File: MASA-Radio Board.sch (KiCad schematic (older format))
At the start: 47 parts, among them IC1 FAN4010IL6X_F113, IC2 FAN4010IL6X_F113, J1 SC_19-20, J2 Conn_01x03_Male, J3 Conn_01x02, J4 Conn_01x06, J5 Conn_01x06, J6 Conn_01x02, J7 UJ2-MBH-1-SMT-TR, J8 Conn_01x02_Male, U1 MP5077GG-Z, U2 MIC5504-3.3YM5-TR, U3 BL654PA, U4 XBP9B-DPST-001, U6 MP5077GG-Z

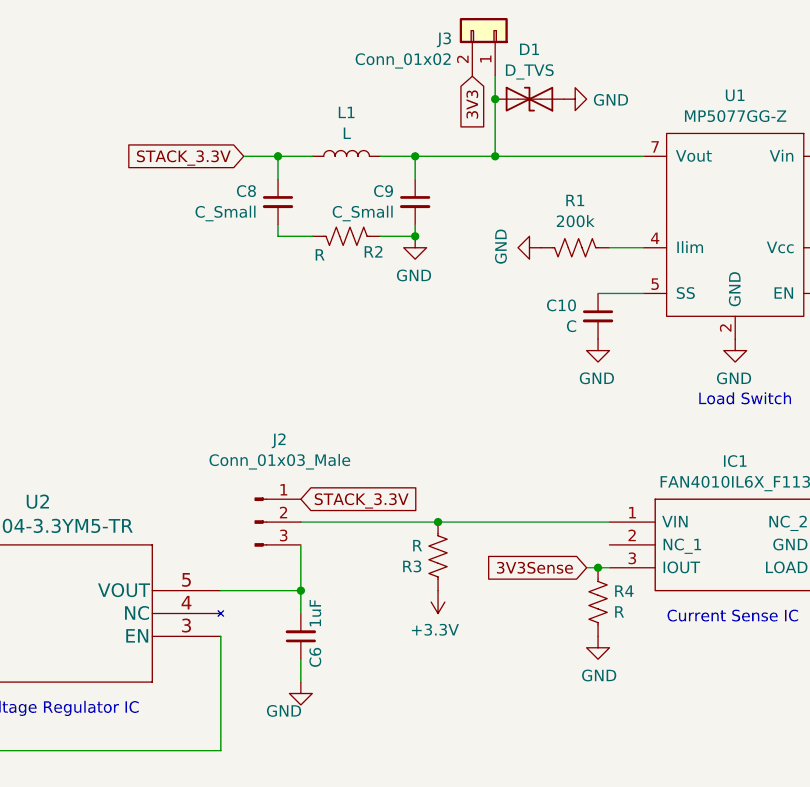
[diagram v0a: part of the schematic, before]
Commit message: Updated R/Cap values
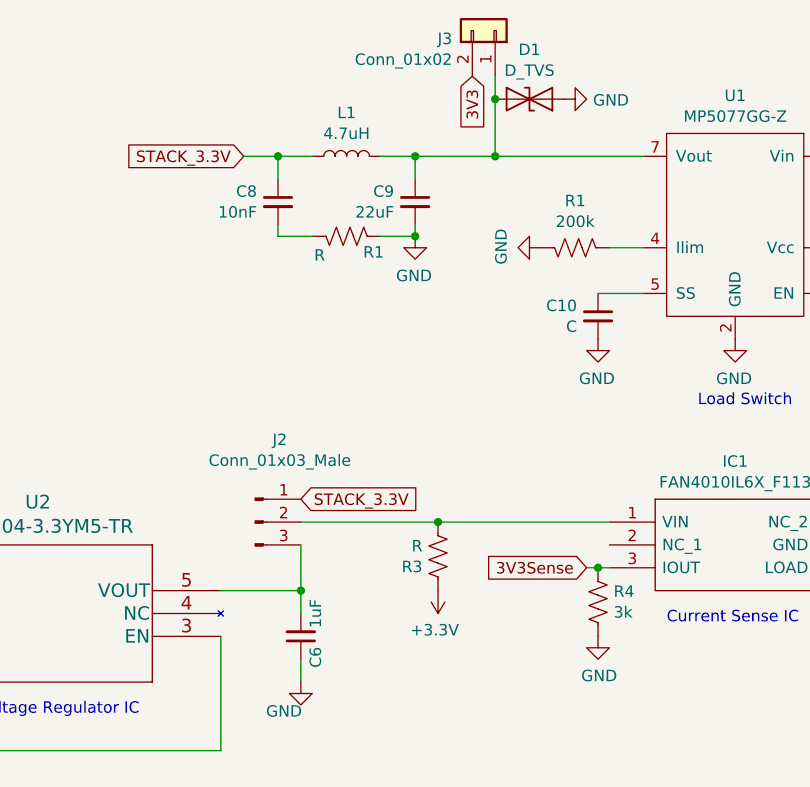
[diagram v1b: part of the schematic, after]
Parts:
- C8: value C_Small -> 10nF
- C9: value C_Small -> 22uF
- L1: value L -> 4.7uH
- R4: value R -> 3k
- renumbered R2 to R1
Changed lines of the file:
@@
 P 6450 4500
 F 0 "R4" H 6518 4546 50  0000 L CNN
-F 1 "R" H 6518 4455 50  0000 L CNN
+F 1 "3k" H 6518 4455 50  0000 L CNN
 F 2 "" V 6490 4490 50  0001 C CNN
 F 3 "~" H 6450 4500 50  0001 C CNN
@@
 	5650 2850 5650 2900
 $Comp
-L Device:R_US R2
+L Device:R_US R1
 U 1 1 5E0D0355
 P 5350 2900
-F 0 "R2" V 5280 3018 50  0000 C CNN
+F 0 "R1" V 5280 3018 50  0000 C CNN
 F 1 "R" V 5267 2782 50  0000 C CNN
 F 2 "" V 5390 2890 50  0001 C CNN
@@
 P 5350 2550
 F 0 "L1" V 5540 2550 50  0000 C CNN
-F 1 "L" V 5449 2550 50  0000 C CNN
+F 1 "4.7uH" V 5449 2550 50  0000 C CNN
 F 2 "" H 5350 2550 50  0001 C CNN
 F 3 "~" H 5350 2550 50  0001 C CNN
@@
 P 5650 2750
 F 0 "C9" H 5742 2796 50  0000 L CNN
-F 1 "C_Small" H 5742 2705 50  0000 L CNN
+F 1 "22uF" H 5742 2705 50  0000 L CNN
 F 2 "" H 5650 2750 50  0001 C CNN
 F 3 "~" H 5650 2750 50  0001 C CNN
@@
 P 5050 2750
 F 0 "C8" H 5142 2796 50  0000 L CNN
-F 1 "C_Small" H 5142 2705 50  0000 L CNN
+F 1 "10nF" H 5142 2705 50  0000 L CNN
 F 2 "" H 5050 2750 50  0001 C CNN
 F 3 "~" H 5050 2750 50  0001 C CNN

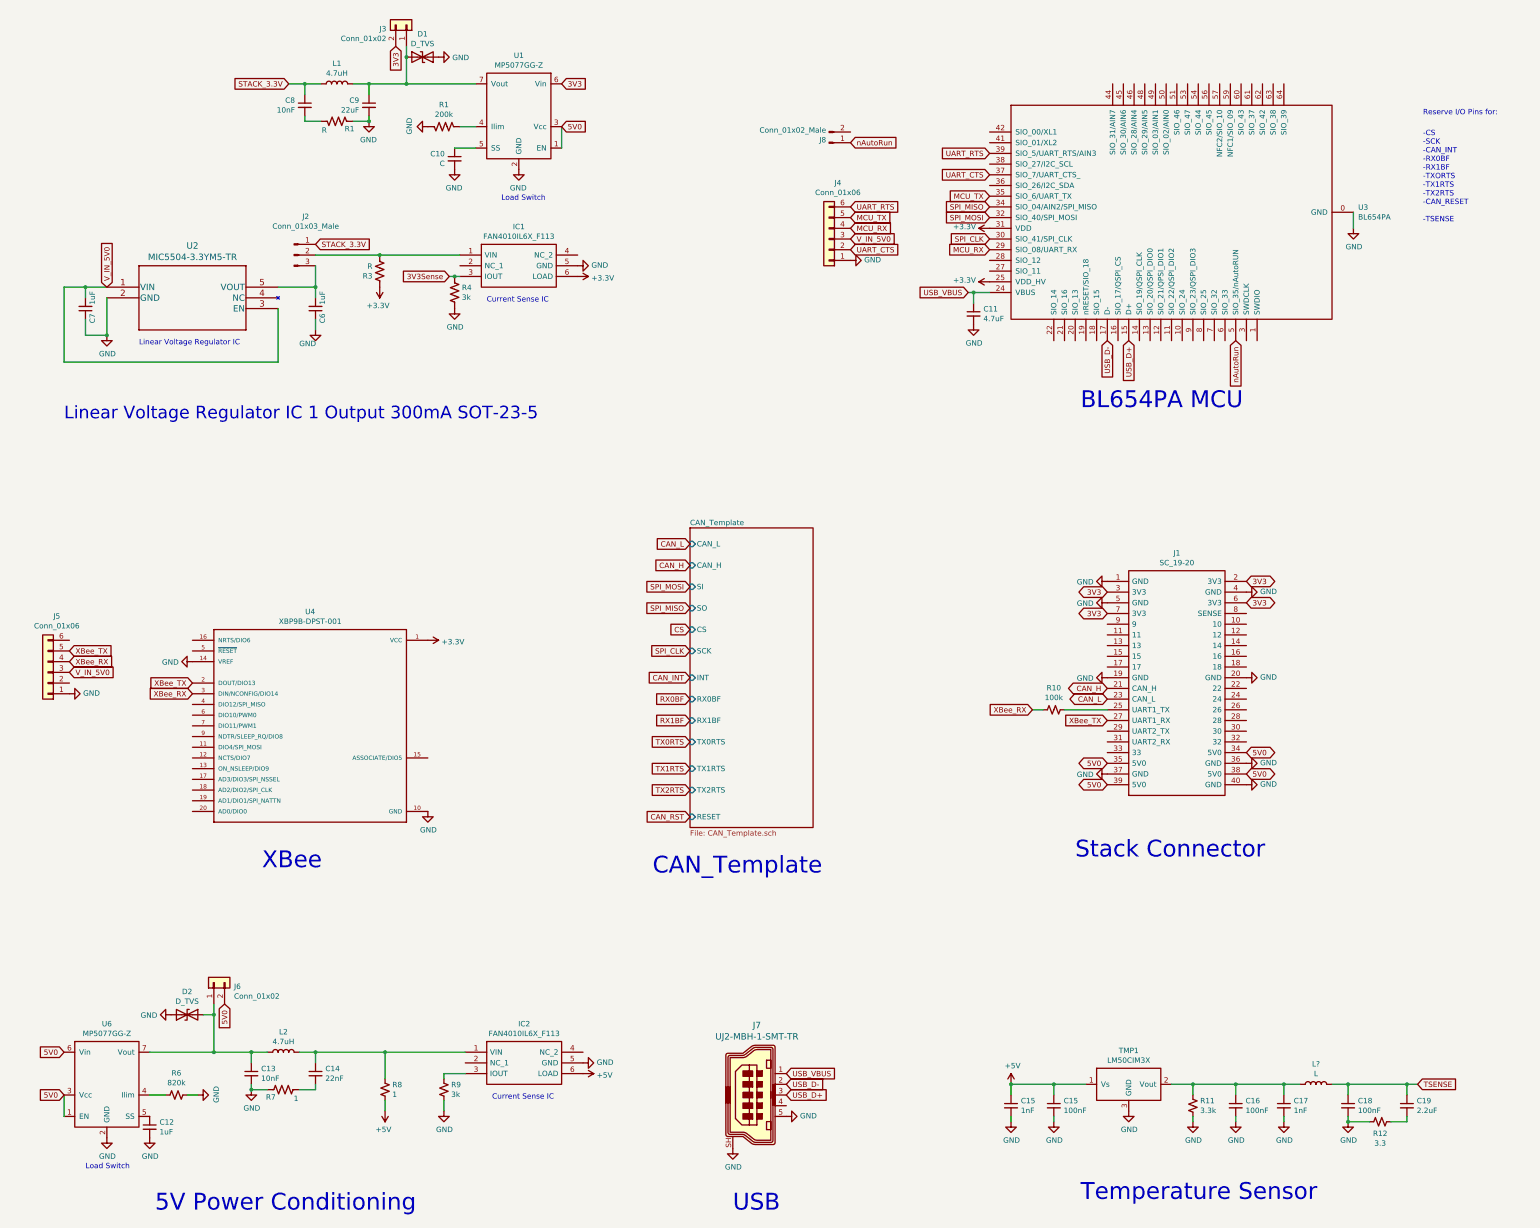
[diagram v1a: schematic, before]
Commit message: Some minor footprint and value updates - unfinished
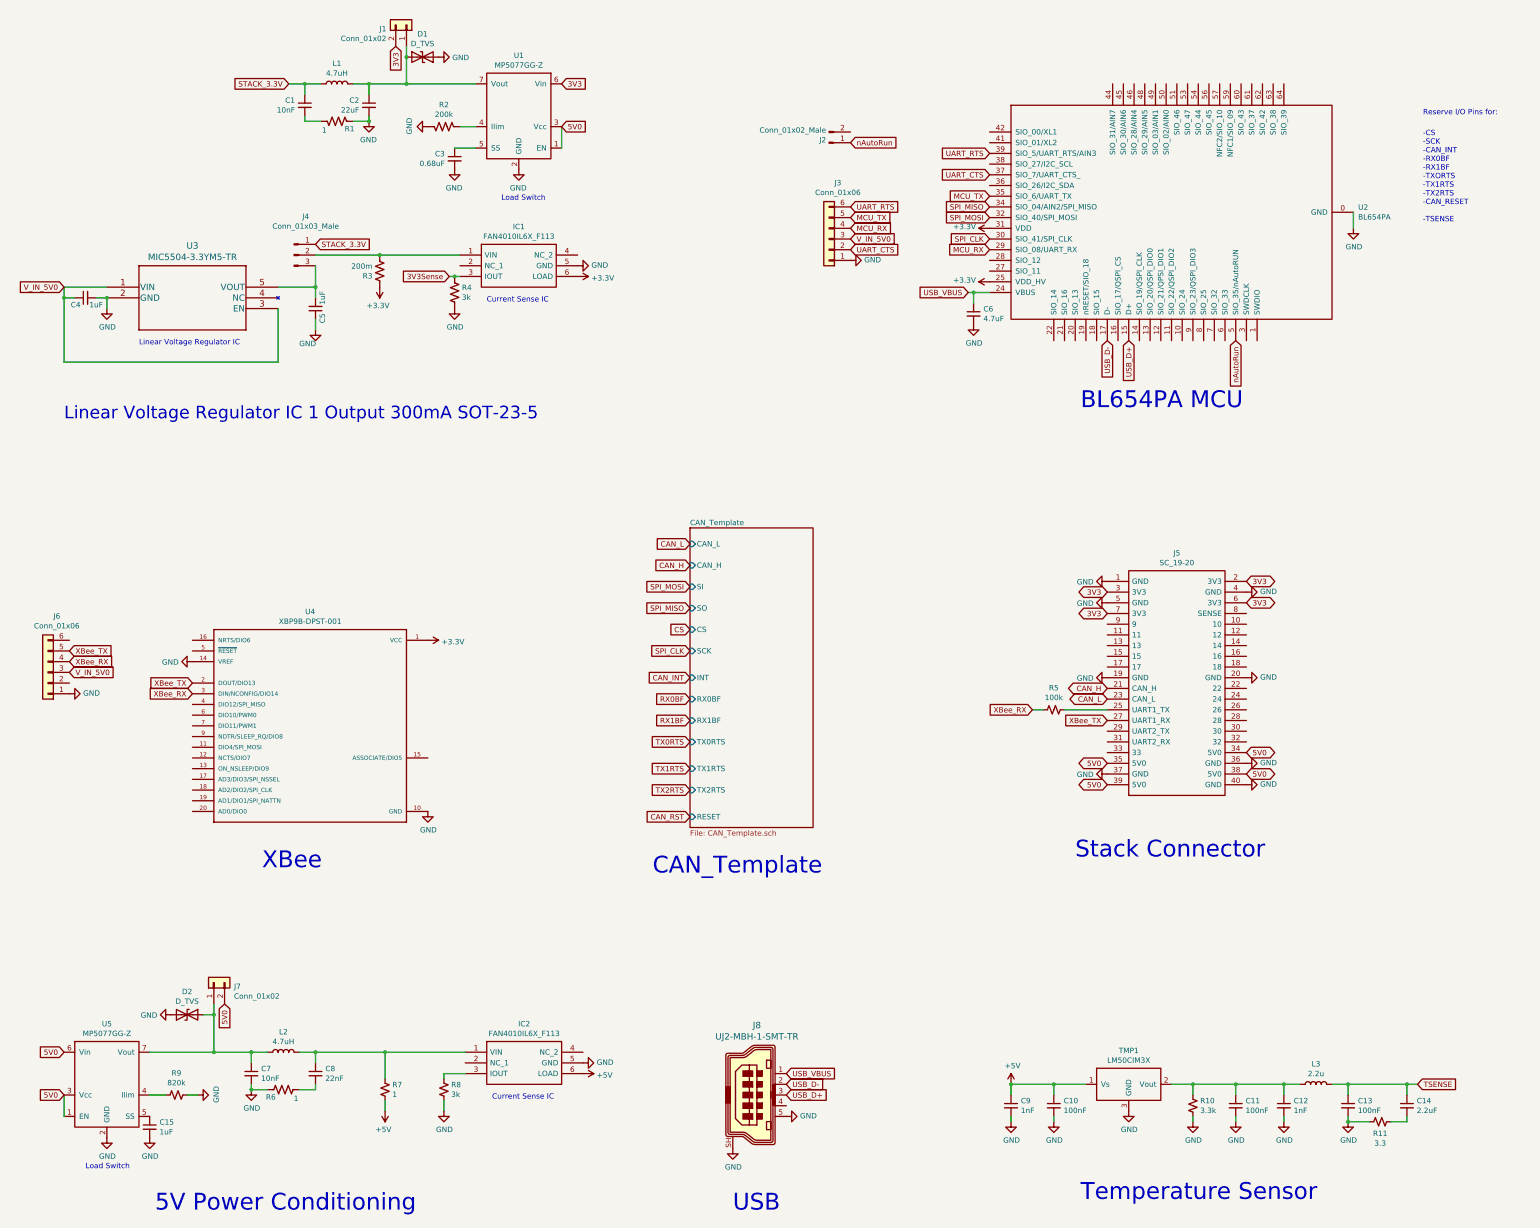
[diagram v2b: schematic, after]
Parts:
- C1: renamed from C8; footprint (none) -> Capacitor_SMD:C_0402_1005Metric
- C10, C9: renamed from C15; footprint (none) -> Capacitor_SMD:C_0805_2012Metric
- C11: renamed from C16; footprint (none) -> Capacitor_SMD:C_0805_2012Metric
- C12: renamed from C17; footprint (none) -> Capacitor_SMD:C_0805_2012Metric
- C13: renamed from C18; footprint (none) -> Capacitor_SMD:C_0805_2012Metric
- C14: renamed from C19; footprint (none) -> Capacitor_SMD:C_0805_2012Metric
- C15: renamed from C12; footprint (none) -> Capacitor_SMD:C_0805_2012Metric
- C2: renamed from C9; footprint (none) -> Capacitor_SMD:C_0805_2012Metric
- C3: renamed from C10; value C -> 0.68uF; footprint (none) -> Capacitor_SMD:C_0805_2012Metric
- C4: renamed from C7; footprint (none) -> Capacitor_SMD:C_0805_2012Metric
- C5: renamed from C6; footprint (none) -> Capacitor_SMD:C_0805_2012Metric
- C6: renamed from C11; footprint (none) -> Capacitor_SMD:C_0805_2012Metric
- C7: renamed from C13; footprint (none) -> Capacitor_SMD:C_0402_1005Metric
- C8: renamed from C14; footprint (none) -> Capacitor_SMD:C_0805_2012Metric
- L1, L2: footprint (none) -> Inductor_SMD:L_0805_2012Metric
- L3: renamed from L?; value L -> 2.2u; footprint (none) -> Inductor_SMD:L_0805_2012Metric
- R1: value R -> 1; footprint (none) -> Resistor_SMD:R_0402_1005Metric
- R10: renamed from R11; footprint (none) -> Resistor_SMD:R_0805_2012Metric
- R11: renamed from R12; footprint (none) -> Resistor_SMD:R_0805_2012Metric
- R2: renamed from R1; footprint (none) -> Resistor_SMD:R_0805_2012Metric
- R3: value R -> 200m; footprint (none) -> Resistor_SMD:R_0805_2012Metric
- R4: footprint (none) -> Resistor_SMD:R_0805_2012Metric
- R5: renamed from R10; footprint (none) -> Resistor_SMD:R_0805_2012Metric
- R6: renamed from R7; footprint (none) -> Resistor_SMD:R_0402_1005Metric
- R7: renamed from R8; footprint (none) -> Resistor_SMD:R_0805_2012Metric
- R8: renamed from R9; footprint (none) -> Resistor_SMD:R_0805_2012Metric
- R9: renamed from R6; footprint (none) -> Resistor_SMD:R_0805_2012Metric
- renumbered J3 to J1, J8 to J2, J4 to J3, J2 to J4, J1 to J5, J5 to J6, J6 to J7, J7 to J8, U3 to U2, U2 to U3, U6 to U5
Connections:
- net GND: now also C4.2; no longer C4.1
- net V_IN_5V0: now also C4.1; no longer C4.2
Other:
- moved on the sheet: C4

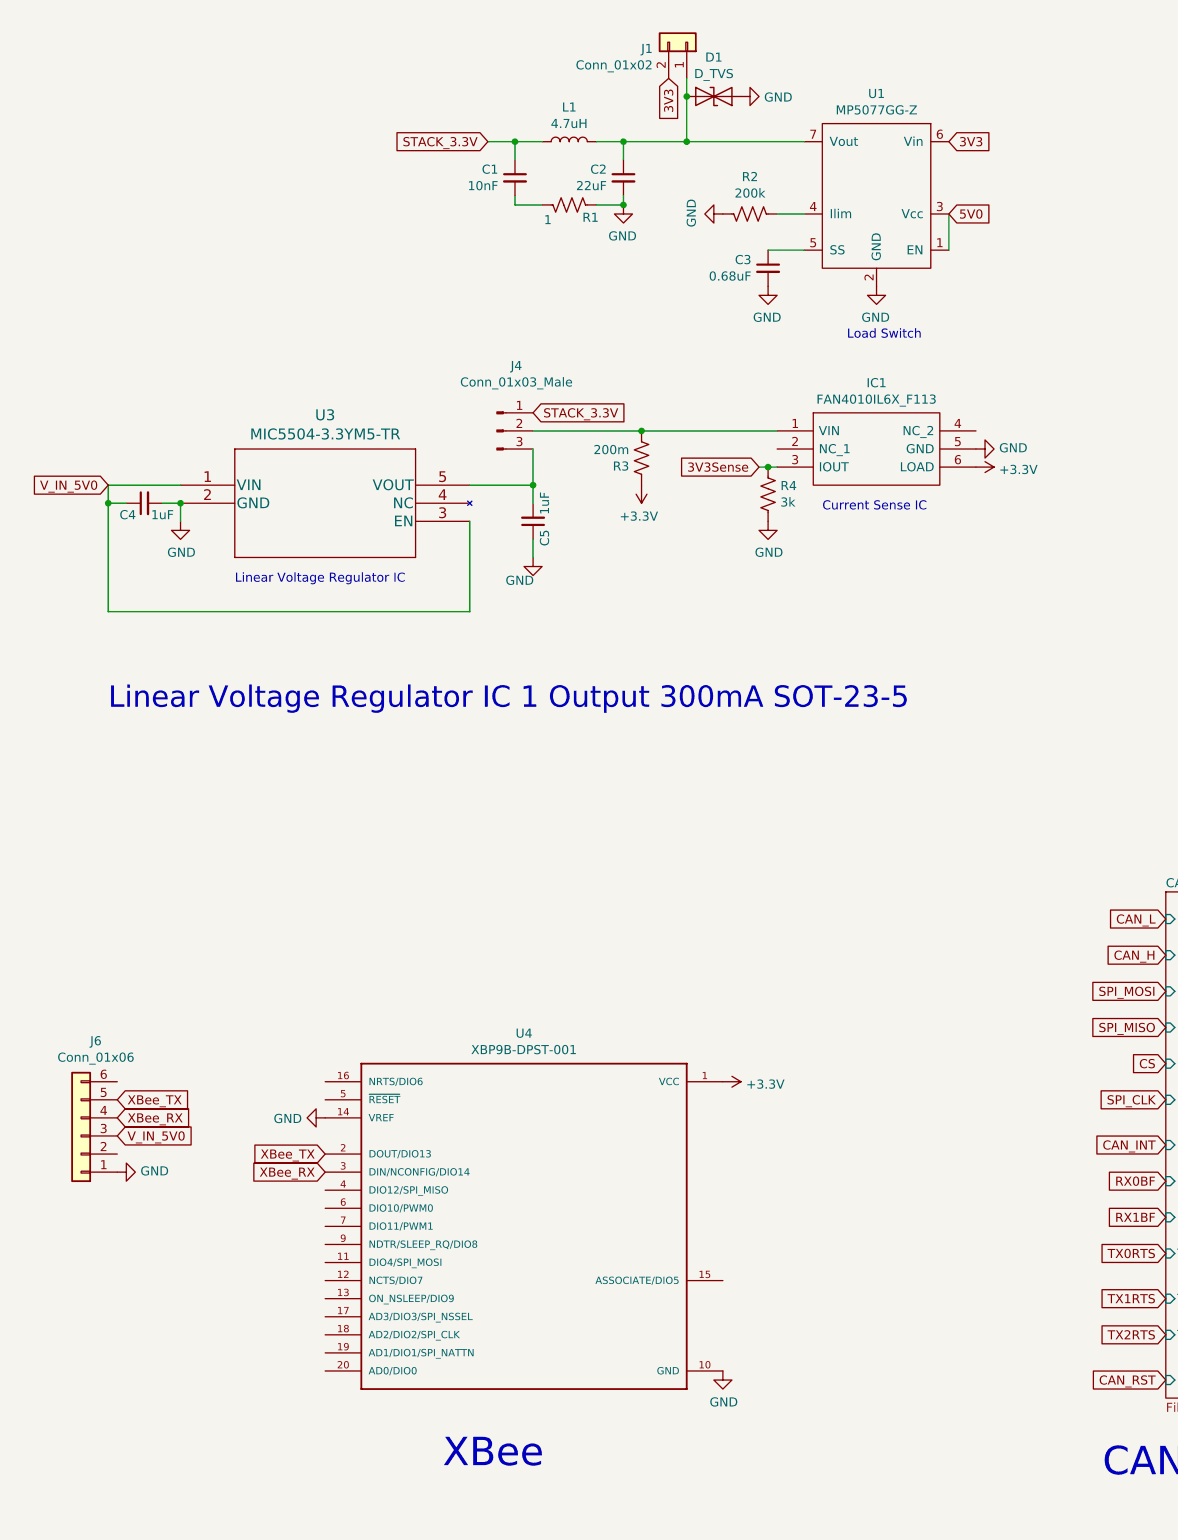
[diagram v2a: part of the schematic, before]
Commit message: Updated footprints, began board layout, board layers
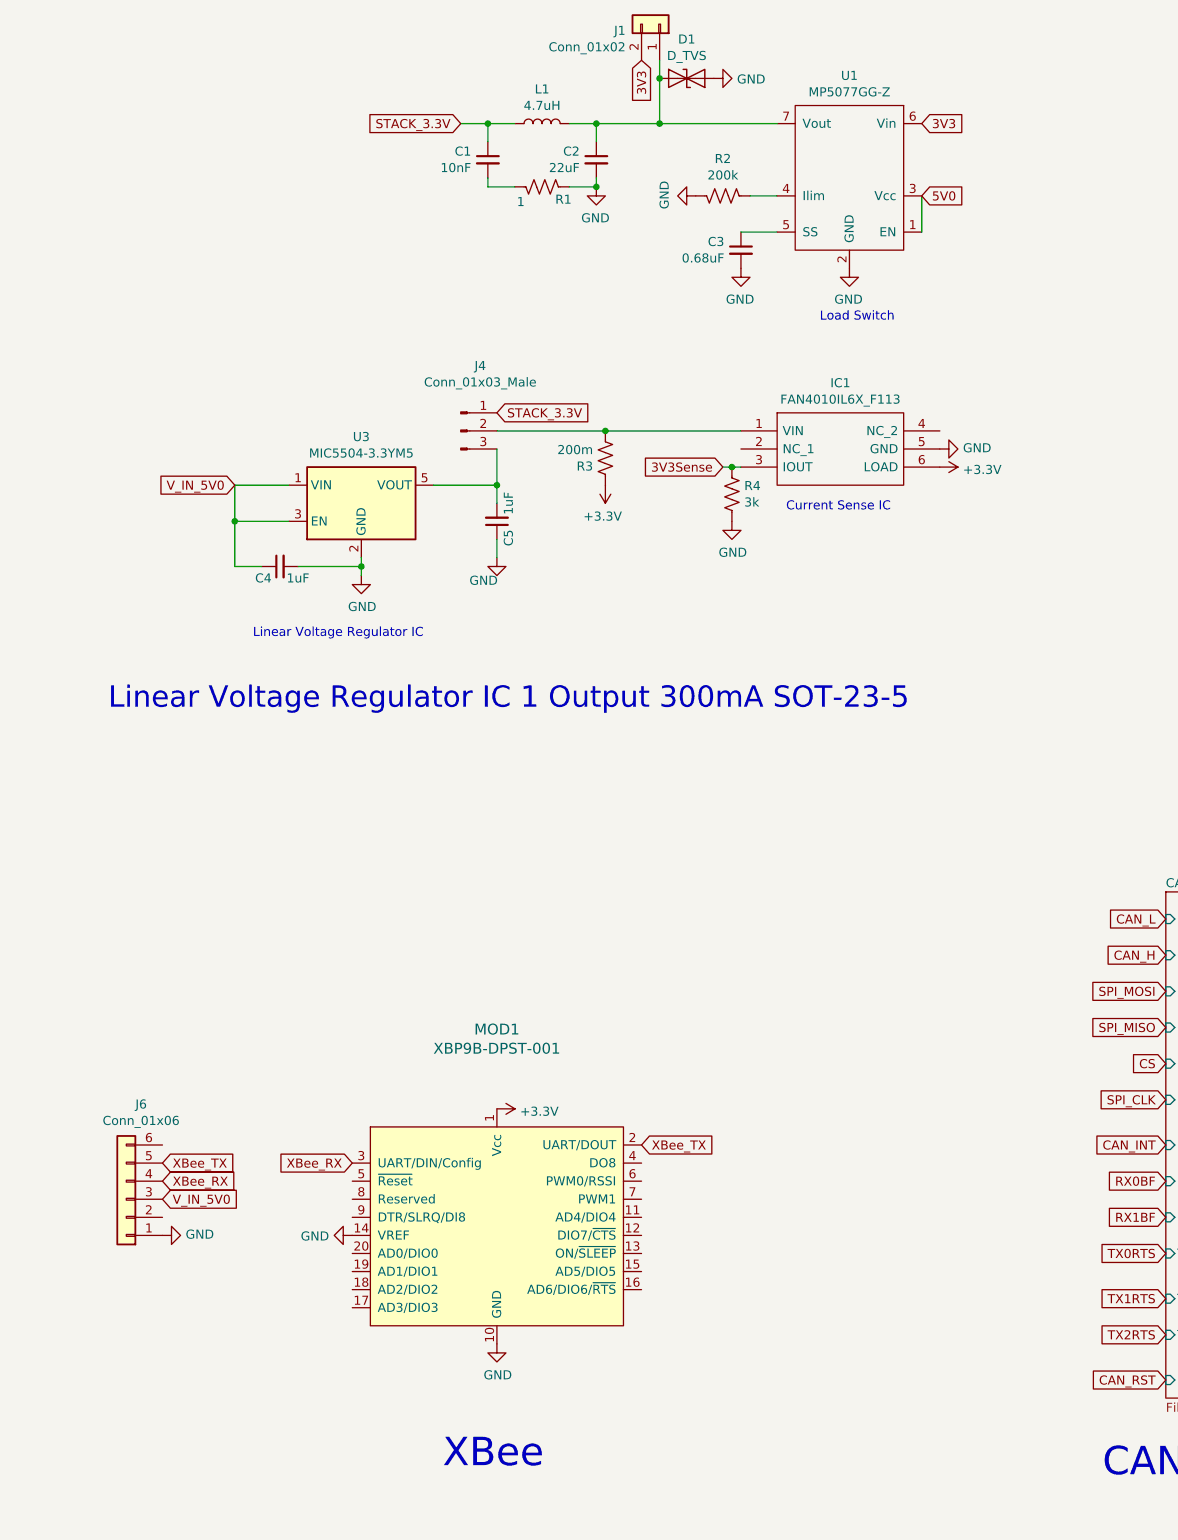
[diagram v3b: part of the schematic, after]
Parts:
- removed U3: MIC5504-3.3YM5-TR, SOT-23-5_MC, symbol MIC5504-3.3YM5-TR:MIC5504-3.3YM5-TR
- removed U4: XBP9B-DPST-001, DIP2200W51P200L3294H279Q20P, symbol MASA-Radio-Board-rescue:XBP9B-DPST-001-XBP9B-DPST-001
- added MOD1: XBP9B-DPST-001, digikey-footprints:XBEE_PRO-20_THT, symbol dk_RF-Transceiver-Modules:XBP9B-DPST-001
- added U3: MIC5504-3.3YM5, Package_TO_SOT_SMD:SOT-23-5, symbol Regulator_Linear:MIC5504-3.3YM5
- D1, D2: footprint (none) -> Diode_SMD:D_SOD-523
- IC1, IC2: footprint 6-LEAD_MICROPAK -> MASA_Library:6-LEAD_MICROPAK
- J1, J2, J7: footprint (none) -> Connector_PinHeader_2.54mm:PinHeader_1x02_P2.54mm_Vertical
- J3, J6: footprint (none) -> Connector_PinHeader_2.54mm:PinHeader_1x06_P2.54mm_Vertical
- J4: footprint (none) -> Connector_PinHeader_2.54mm:PinHeader_1x03_P2.54mm_Vertical
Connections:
- net +3V3: now also MOD1.1 (Vcc)
- net GND: now also MOD1.10 (GND), MOD1.14 (VREF), U3.2 (GND)
- net V_IN_5V0: now also U3.1 (VIN), U3.3 (EN)
- net XBee_RX: now also MOD1.3 (UART/DIN/Config)
- net XBee_TX: now also MOD1.2 (UART/DOUT)
- net at C5.2, J4.3 (Pin_3): now also U3.5 (VOUT)
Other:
- moved on the sheet: C1, C2, C3, C4, C5, D1, IC1, J1, J4, J6, L1, R1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
